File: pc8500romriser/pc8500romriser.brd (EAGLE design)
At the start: 21 x 43 mm, 5 parts, among them CON1 HN27C101AG, U1 SST39VF010-70-4I-WHETSOP32_WH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

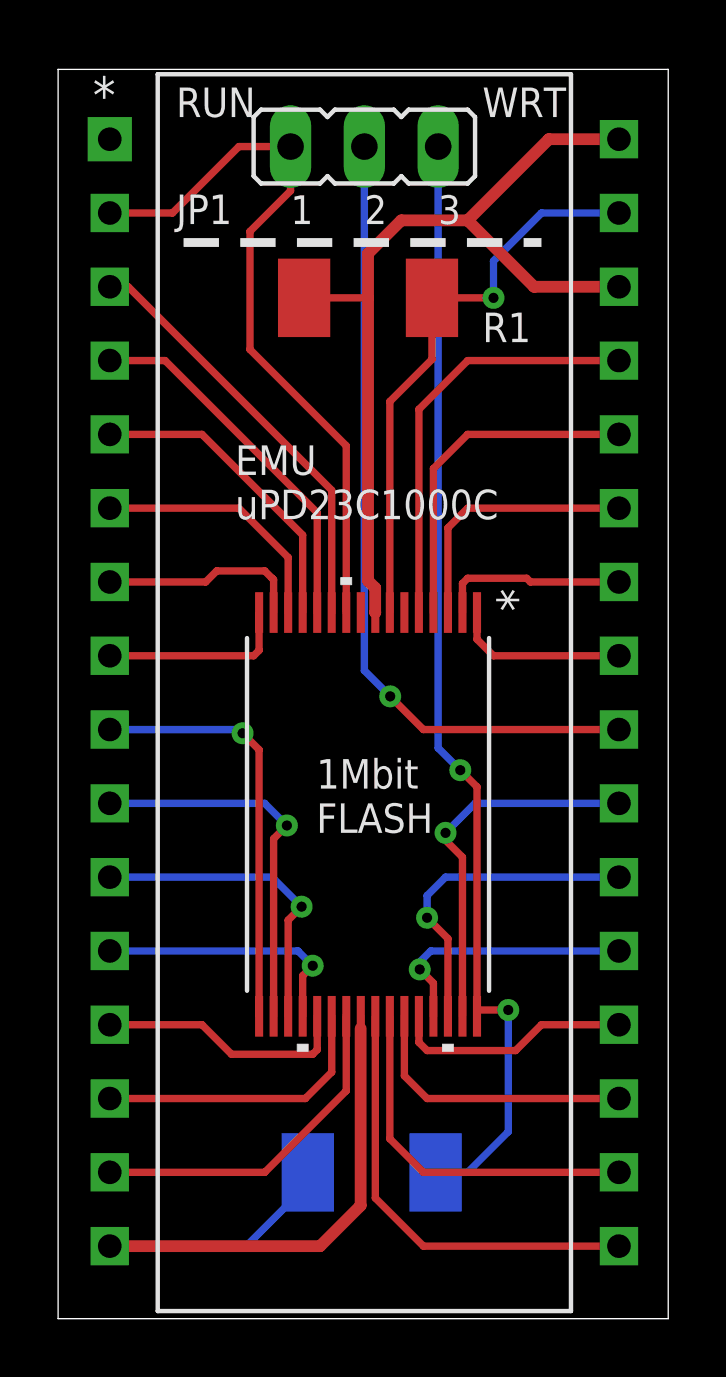
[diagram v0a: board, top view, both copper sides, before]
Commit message: Adjusted routing signal lines.
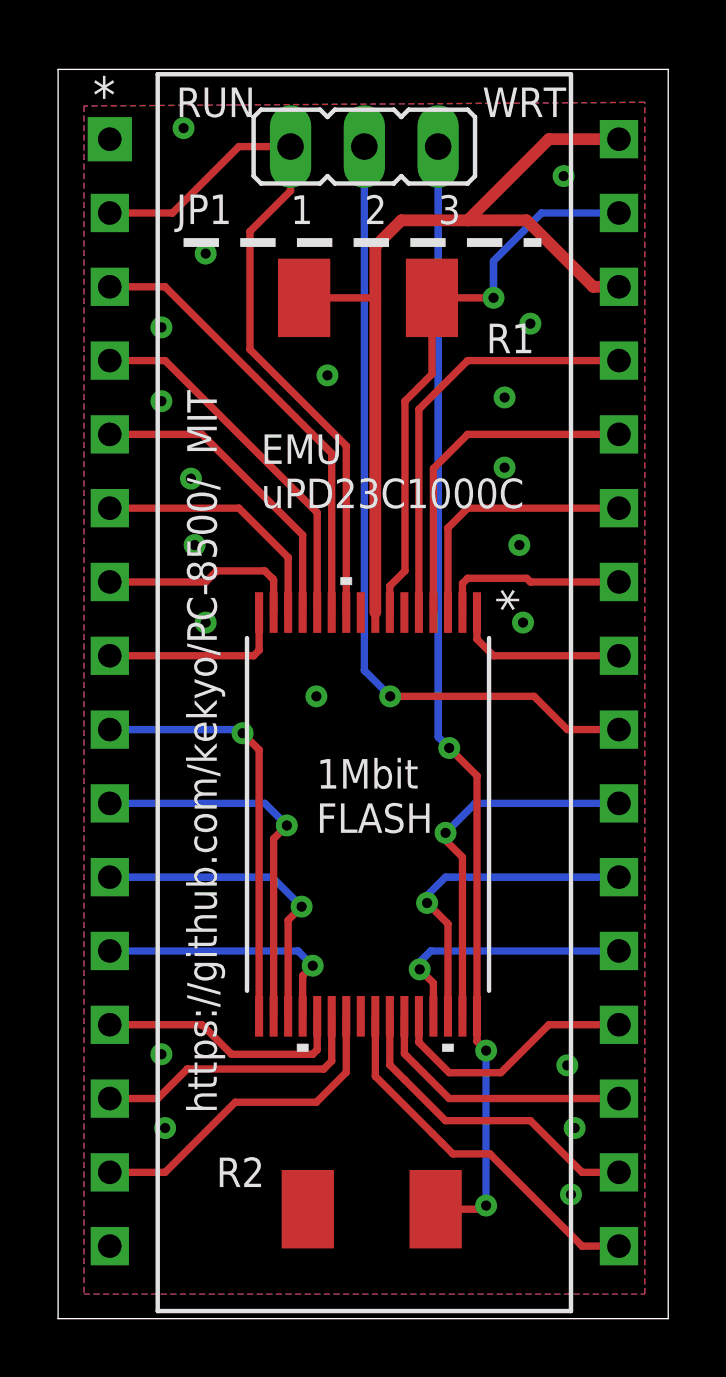
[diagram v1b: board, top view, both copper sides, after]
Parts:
- moved R2 1.27 mm to (10.8, 40.8), flipped to the top, turned to 180 degrees
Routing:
- net GND: track 23.8 -> 0.42 mm, vias 0 -> 20
- net D3: track 15.3 -> 12.9 mm
- net D4: track 12.6 -> 11.1 mm
- net A15: track 14.7 -> 15.5 mm
- net D6: track 8.27 -> 8.90 mm
- net /OE: track 38.8 -> 38.9 mm, vias 2 -> 3
- added copper zone on layer 1, net GND
- added copper zone on layer 16, net GND
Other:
- board text added: "https://github.com/kekyo/PC-8500/ MIT"
